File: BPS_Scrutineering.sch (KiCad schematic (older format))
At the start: 22 parts, among them J1 Conn_01x01_Female, J10 Conn_01x01_Female, J11 Conn_01x01_Female, J12 Conn_01x01_Female, J13 Conn_01x01_Female, J14 Conn_01x01_Female, J2 Conn_01x01_Female, J3 Conn_01x01_Female, J4 Conn_01x01_Female, J5 Conn_01x01_Female, J6 Conn_01x01_Female, J7 Conn_01x01_Female, J8 Conn_01x01_Female, J9 Conn_01x01_Female, SW1 SW_DIP_x07, SW2 SW_DIP_x07

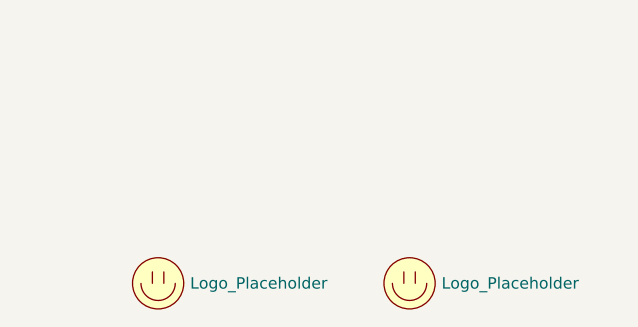
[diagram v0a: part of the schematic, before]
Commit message: Adds names and adds labels to logos on schematic
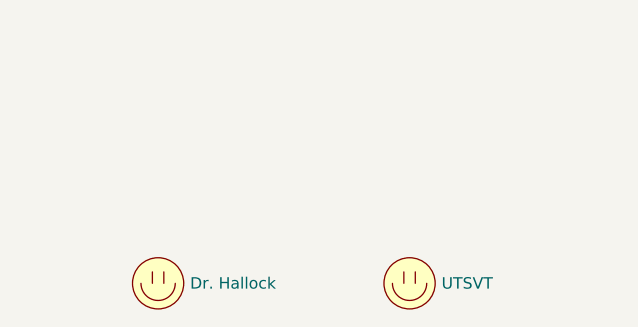
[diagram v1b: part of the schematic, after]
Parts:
- Dr_Hallock1: value Logo_Placeholder -> Dr. Hallock
- JC1, JC2, JC3, JC4: footprint Connector_Molex:Molex_Micro-Fit_3.0_43650-0700_1x07_P3.00mm_Horizontal -> UTSVT_Connectors:Molex_MicroFit_01x07_Horizontal
- UTSVT_Logo1: value Logo_Placeholder -> UTSVT
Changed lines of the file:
@@
 F 0 "JC3" H 4058 4431 50  0000 C CNN
 F 1 "Conn_01x07" H 4058 4340 50  0000 C CNN
-F 2 "Connector_Molex:Molex_Micro-Fit_3.0_43650-0700_1x07_P3.00mm_Horizontal" H 3950 3950 50  0001 C CNN
+F 2 "UTSVT_Connectors:Molex_MicroFit_01x07_Horizontal" H 3950 3950 50  0001 C CNN
 F 3 "~" H 3950 3950 50  0001 C CNN
 	1    3950 3950
@@
 F 0 "JC2" H 7550 2400 50  0000 R CNN
 F 1 "Conn_01x07" H 7700 2500 50  0000 R CNN
-F 2 "Connector_Molex:Molex_Micro-Fit_3.0_43650-0700_1x07_P3.00mm_Horizontal" H 7550 2900 50  0001 C CNN
+F 2 "UTSVT_Connectors:Molex_MicroFit_01x07_Horizontal" H 7550 2900 50  0001 C CNN
 F 3 "~" H 7550 2900 50  0001 C CNN
 	1    7550 2900
@@
 F 0 "JC4" H 7650 3550 50  0000 R CNN
 F 1 "Conn_01x07" H 7900 4400 50  0000 R CNN
-F 2 "Connector_Molex:Molex_Micro-Fit_3.0_43650-0700_1x07_P3.00mm_Horizontal" H 7550 3950 50  0001 C CNN
+F 2 "UTSVT_Connectors:Molex_MicroFit_01x07_Horizontal" H 7550 3950 50  0001 C CNN
 F 3 "~" H 7550 3950 50  0001 C CNN
 	1    7550 3950
@@
 F 0 "JC1" H 4058 3381 50  0000 C CNN
 F 1 "Conn_01x07" H 4058 3290 50  0000 C CNN
-F 2 "Connector_Molex:Molex_Micro-Fit_3.0_43650-0700_1x07_P3.00mm_Horizontal" H 3950 2900 50  0001 C CNN
+F 2 "UTSVT_Connectors:Molex_MicroFit_01x07_Horizontal" H 3950 2900 50  0001 C CNN
 F 3 "~" H 3950 2900 50  0001 C CNN
 	1    3950 2900
@@
 P 8700 6050
 F 0 "UTSVT_Logo1" H 8700 6200 50  0001 C CNN
-F 1 "Logo_Placeholder" H 8840 6050 50  0000 L CNN
+F 1 "UTSVT" H 8840 6050 50  0000 L CNN
 F 2 "UTSVT_Special:UTSVT_Logo_Symbol" H 8700 6125 50  0001 C CNN
 F 3 "" H 8700 6125 50  0001 C CNN
@@
 P 7600 6050
 F 0 "Dr_Hallock1" H 7600 6200 50  0001 C CNN
-F 1 "Logo_Placeholder" H 7740 6050 50  0000 L CNN
+F 1 "Dr. Hallock" H 7740 6050 50  0000 L CNN
 F 2 "UTSVT_Special:Hallock_Image" H 7600 6125 50  0001 C CNN
 F 3 "" H 7600 6125 50  0001 C CNN
